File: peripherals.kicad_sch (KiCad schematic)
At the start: 41 parts, among them J8 Conn_01x06_Male, J9 Conn_01x04_MountingPin, U1 MIMX8MM6DVTLZAA, U30 74LVC2G07, U31 TXB0104RUT, U32 TCA9803

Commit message: change USB-UART conn, add new 0402 fp, more pcb work
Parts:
- C143, C144, C145, C146, C147: footprint Capacitor_SMD:C_0402_1005Metric -> qsbc:C_0402_1005Metric
- R100, R101, R102, R103, R104, R105, R106, R107, R108, R109, R110, R111, R112, R113, R114, R115, R116, R117, R118, R119, R120, R121, R122, R123, R124, R125, R126: footprint Resistor_SMD:R_0402_1005Metric -> qsbc:R_0402_1005Metric
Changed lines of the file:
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@@
       (effects (font (size 1.27 1.27)) (justify left))
     )
-    (property "Footprint" "Resistor_SMD:R_0402_1005Metric" (id 2) (at 205.232 40.64 90)
+    (property "Footprint" "qsbc:R_0402_1005Metric" (id 2) (at 205.232 40.64 90)
       (effects (font (size 1.27 1.27)) hide)
     )
@@
       (effects (font (size 1.27 1.27)) (justify left))
     )
-    (property "Footprint" "Resistor_SMD:R_0402_1005Metric" (id 2) (at 125.222 227.33 90)
+    (property "Footprint" "qsbc:R_0402_1005Metric" (id 2) (at 125.222 227.33 90)
       (effects (font (size 1.27 1.27)) hide)
     )
@@
       (effects (font (size 1.27 1.27)) (justify left))
     )
-    (property "Footprint" "Resistor_SMD:R_0402_1005Metric" (id 2) (at 135.382 227.33 90)
+    (property "Footprint" "qsbc:R_0402_1005Metric" (id 2) (at 135.382 227.33 90)
       (effects (font (size 1.27 1.27)) hide)
     )
@@
       (effects (font (size 1.27 1.27)) (justify left))
     )
-    (property "Footprint" "Resistor_SMD:R_0402_1005Metric" (id 2) (at 174.752 40.64 90)
+    (property "Footprint" "qsbc:R_0402_1005Metric" (id 2) (at 174.752 40.64 90)
       (effects (font (size 1.27 1.27)) hide)
     )
@@
       (effects (font (size 1.27 1.27)) (justify left))
     )
-    (property "Footprint" "Resistor_SMD:R_0402_1005Metric" (id 2) (at 168.402 107.95 90)
+    (property "Footprint" "qsbc:R_0402_1005Metric" (id 2) (at 168.402 107.95 90)
       (effects (font (size 1.27 1.27)) hide)
     )
@@
       (effects (font (size 1.27 1.27)) (justify left))
     )
-    (property "Footprint" "Resistor_SMD:R_0402_1005Metric" (id 2) (at 200.152 40.64 90)
+    (property "Footprint" "qsbc:R_0402_1005Metric" (id 2) (at 200.152 40.64 90)
       (effects (font (size 1.27 1.27)) hide)
     )
@@
       (effects (font (size 1.27 1.27)) (justify left))
     )
-    (property "Footprint" "Resistor_SMD:R_0402_1005Metric" (id 2) (at 195.072 40.64 90)
+    (property "Footprint" "qsbc:R_0402_1005Metric" (id 2) (at 195.072 40.64 90)
       (effects (font (size 1.27 1.27)) hide)
     )
@@
       (effects (font (size 1.27 1.27)) (justify left))
     )
-    (property "Footprint" "Capacitor_SMD:C_0402_1005Metric" (id 2) (at 220.6752 118.11 0)
+    (property "Footprint" "qsbc:C_0402_1005Metric" (id 2) (at 220.6752 118.11 0)
       (effects (font (size 1.27 1.27)) hide)
     )
@@
       (effects (font (size 1.27 1.27)) (justify left))
     )
-    (property "Footprint" "Resistor_SMD:R_0402_1005Metric" (id 2) (at 104.902 227.33 90)
+    (property "Footprint" "qsbc:R_0402_1005Metric" (id 2) (at 104.902 227.33 90)
       (effects (font (size 1.27 1.27)) hide)
     )
@@
       (effects (font (size 1.27 1.27)) (justify left))
     )
-    (property "Footprint" "Resistor_SMD:R_0402_1005Metric" (id 2) (at 189.992 40.64 90)
+    (property "Footprint" "qsbc:R_0402_1005Metric" (id 2) (at 189.992 40.64 90)
       (effects (font (size 1.27 1.27)) hide)
     )
@@
       (effects (font (size 1.27 1.27)) (justify left))
     )
-    (property "Footprint" "Resistor_SMD:R_0402_1005Metric" (id 2) (at 174.752 191.77 90)
+    (property "Footprint" "qsbc:R_0402_1005Metric" (id 2) (at 174.752 191.77 90)
       (effects (font (size 1.27 1.27)) hide)
     )
@@
       (effects (font (size 1.27 1.27)) (justify left))
     )
-    (property "Footprint" "Capacitor_SMD:C_0402_1005Metric" (id 2) (at 249.8852 181.61 0)
+    (property "Footprint" "qsbc:C_0402_1005Metric" (id 2) (at 249.8852 181.61 0)
       (effects (font (size 1.27 1.27)) hide)
     )
@@
       (effects (font (size 1.27 1.27)) (justify left))
     )
-    (property "Footprint" "Resistor_SMD:R_0402_1005Metric" (id 2) (at 115.062 227.33 90)
+    (property "Footprint" "qsbc:R_0402_1005Metric" (id 2) (at 115.062 227.33 90)
       (effects (font (size 1.27 1.27)) hide)
     )
@@
       (effects (font (size 1.27 1.27)) (justify left))
     )
-    (property "Footprint" "Resistor_SMD:R_0402_1005Metric" (id 2) (at 145.542 227.33 90)
+    (property "Footprint" "qsbc:R_0402_1005Metric" (id 2) (at 145.542 227.33 90)
       (effects (font (size 1.27 1.27)) hide)
     )
@@
       (effects (font (size 1.27 1.27)) (justify left))
     )
-    (property "Footprint" "Resistor_SMD:R_0402_1005Metric" (id 2) (at 211.582 227.33 90)
+    (property "Footprint" "qsbc:R_0402_1005Metric" (id 2) (at 211.582 227.33 90)
       (effects (font (size 1.27 1.27)) hide)
     )
@@
       (effects (font (size 1.27 1.27)) (justify left))
     )
-    (property "Footprint" "Resistor_SMD:R_0402_1005Metric" (id 2) (at 186.182 107.95 90)
+    (property "Footprint" "qsbc:R_0402_1005Metric" (id 2) (at 186.182 107.95 90)
       (effects (font (size 1.27 1.27)) hide)
     )
@@
       (effects (font (size 1.27 1.27)) (justify left))
     )
-    (property "Footprint" "Capacitor_SMD:C_0402_1005Metric" (id 2) (at 237.1852 181.61 0)
+    (property "Footprint" "qsbc:C_0402_1005Metric" (id 2) (at 237.1852 181.61 0)
       (effects (font (size 1.27 1.27)) hide)
     )
@@
       (effects (font (size 1.27 1.27)) (justify left))
     )
-    (property "Footprint" "Resistor_SMD:R_0402_1005Metric" (id 2) (at 169.672 40.64 90)
+    (property "Footprint" "qsbc:R_0402_1005Metric" (id 2) (at 169.672 40.64 90)
       (effects (font (size 1.27 1.27)) hide)
     )
@@
       (effects (font (size 1.27 1.27)) (justify left))
     )
-    (property "Footprint" "Resistor_SMD:R_0402_1005Metric" (id 2) (at 230.632 40.64 90)
+    (property "Footprint" "qsbc:R_0402_1005Metric" (id 2) (at 230.632 40.64 90)
       (effects (font (size 1.27 1.27)) hide)
     )
@@
       (effects (font (size 1.27 1.27)) (justify left))
     )
-    (property "Footprint" "Resistor_SMD:R_0402_1005Metric" (id 2) (at 201.422 227.33 90)
+    (property "Footprint" "qsbc:R_0402_1005Metric" (id 2) (at 201.422 227.33 90)
       (effects (font (size 1.27 1.27)) hide)
     )
@@
       (effects (font (size 1.27 1.27)) (justify left))
     )
-    (property "Footprint" "Resistor_SMD:R_0402_1005Metric" (id 2) (at 220.472 40.64 90)
+    (property "Footprint" "qsbc:R_0402_1005Metric" (id 2) (at 220.472 40.64 90)
       (effects (font (size 1.27 1.27)) hide)
     )
@@
       (effects (font (size 1.27 1.27)) (justify left))
     )
-    (property "Footprint" "Resistor_SMD:R_0402_1005Metric" (id 2) (at 179.832 40.64 90)
+    (property "Footprint" "qsbc:R_0402_1005Metric" (id 2) (at 179.832 40.64 90)
       (effects (font (size 1.27 1.27)) hide)
     )
@@
       (effects (font (size 1.27 1.27)) (justify left))
     )
-    (property "Footprint" "Capacitor_SMD:C_0402_1005Metric" (id 2) (at 250.2044 231.1951 0)
+    (property "Footprint" "qsbc:C_0402_1005Metric" (id 2) (at 250.2044 231.1951 0)
       (effects (font (size 1.27 1.27)) hide)
     )
@@
       (effects (font (size 1.27 1.27)) (justify left))
     )
-    (property "Footprint" "Capacitor_SMD:C_0402_1005Metric" (id 2) (at 237.5044 231.1951 0)
+    (property "Footprint" "qsbc:C_0402_1005Metric" (id 2) (at 237.5044 231.1951 0)
       (effects (font (size 1.27 1.27)) hide)
     )
@@
       (effects (font (size 1.27 1.27)) (justify left))
     )
-    (property "Footprint" "Resistor_SMD:R_0402_1005Metric" (id 2) (at 225.552 40.64 90)
+    (property "Footprint" "qsbc:R_0402_1005Metric" (id 2) (at 225.552 40.64 90)
       (effects (font (size 1.27 1.27)) hide)
     )
@@
       (effects (font (size 1.27 1.27)) (justify left))
     )
-    (property "Footprint" "Resistor_SMD:R_0402_1005Metric" (id 2) (at 215.392 40.64 90)
+    (property "Footprint" "qsbc:R_0402_1005Metric" (id 2) (at 215.392 40.64 90)
       (effects (font (size 1.27 1.27)) hide)
     )
@@
       (effects (font (size 1.27 1.27)) (justify left))
     )
-    (property "Footprint" "Resistor_SMD:R_0402_1005Metric" (id 2) (at 210.312 40.64 90)
+    (property "Footprint" "qsbc:R_0402_1005Metric" (id 2) (at 210.312 40.64 90)
       (effects (font (size 1.27 1.27)) hide)
     )
@@
       (effects (font (size 1.27 1.27)) (justify left))
     )
-    (property "Footprint" "Resistor_SMD:R_0402_1005Metric" (id 2) (at 159.512 40.64 90)
+    (property "Footprint" "qsbc:R_0402_1005Metric" (id 2) (at 159.512 40.64 90)
       (effects (font (size 1.27 1.27)) hide)
     )
@@
       (effects (font (size 1.27 1.27)) (justify left))
     )
-    (property "Footprint" "Resistor_SMD:R_0402_1005Metric" (id 2) (at 164.592 40.64 90)
+    (property "Footprint" "qsbc:R_0402_1005Metric" (id 2) (at 164.592 40.64 90)
       (effects (font (size 1.27 1.27)) hide)
     )
@@
       (effects (font (size 1.27 1.27)) (justify left))
     )
-    (property "Footprint" "Resistor_SMD:R_0402_1005Metric" (id 2) (at 184.912 40.64 90)
+    (property "Footprint" "qsbc:R_0402_1005Metric" (id 2) (at 184.912 40.64 90)
       (effects (font (size 1.27 1.27)) hide)
     )
@@
       (effects (font (size 1.27 1.27)) (justify left))
     )
-    (property "Footprint" "Resistor_SMD:R_0402_1005Metric" (id 2) (at 94.742 227.33 90)
+    (property "Footprint" "qsbc:R_0402_1005Metric" (id 2) (at 94.742 227.33 90)
       (effects (font (size 1.27 1.27)) hide)
     )
@@
       (effects (font (size 1.27 1.27)) (justify left))
     )
-    (property "Footprint" "Resistor_SMD:R_0402_1005Metric" (id 2) (at 235.712 40.64 90)
+    (property "Footprint" "qsbc:R_0402_1005Metric" (id 2) (at 235.712 40.64 90)
       (effects (font (size 1.27 1.27)) hide)
     )

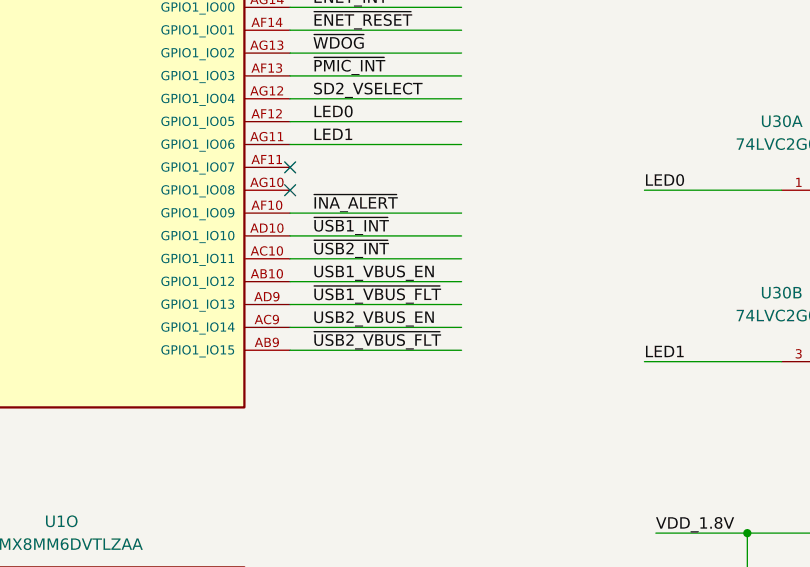
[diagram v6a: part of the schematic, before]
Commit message: swap usb ctrl signals for layout
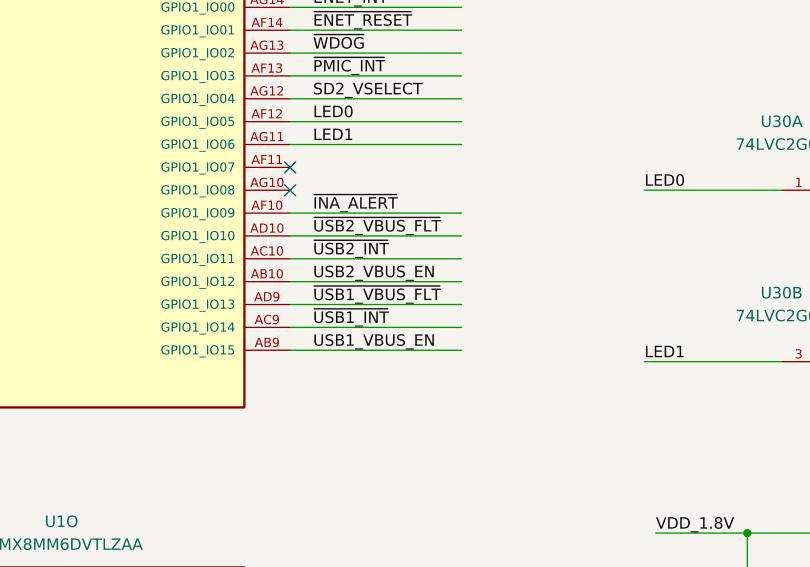
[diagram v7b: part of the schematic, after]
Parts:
- TP27: footprint TestPoint:TestPoint_Pad_D1.0mm -> qsbc:TestPoint_Pad_D0.4mm
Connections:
- net USB1_VBUS_EN: now also U1.AB9 (GPIO1_IO15); no longer U1.AB10 (GPIO1_IO12)
- net USB2_VBUS_EN: now also U1.AB10 (GPIO1_IO12); no longer U1.AC9 (GPIO1_IO14)
- net ~{USB1_INT}: now also U1.AC9 (GPIO1_IO14); no longer U1.AD10 (GPIO1_IO10)
- net ~{USB2_VBUS_FLT}: now also U1.AD10 (GPIO1_IO10); no longer U1.AB9 (GPIO1_IO15)
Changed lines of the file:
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@@
     (effects (font (size 1.27 1.27)) (justify left bottom))
   )
-  (label "~{USB2_VBUS_FLT}" (at 80.01 142.24 0)
+  (label "~{USB2_VBUS_FLT}" (at 80.01 129.54 0)
     (effects (font (size 1.27 1.27)) (justify left bottom))
   )
@@
     (effects (font (size 1.27 1.27)) (justify left bottom))
   )
-  (label "USB2_VBUS_EN" (at 80.01 139.7 0)
+  (label "USB2_VBUS_EN" (at 80.01 134.62 0)
     (effects (font (size 1.27 1.27)) (justify left bottom))
   )
@@
     (effects (font (size 1.27 1.27)) (justify left bottom))
   )
-  (label "USB1_VBUS_EN" (at 80.01 134.62 0)
+  (label "USB1_VBUS_EN" (at 80.01 142.24 0)
     (effects (font (size 1.27 1.27)) (justify left bottom))
   )
@@
     (effects (font (size 1.27 1.27)) (justify left bottom))
   )
-  (label "~{USB1_INT}" (at 80.01 129.54 0)
+  (label "~{USB1_INT}" (at 80.01 139.7 0)
     (effects (font (size 1.27 1.27)) (justify left bottom))
   )
@@
       (effects (font (size 1.27 1.27)) (justify left))
     )
-    (property "Footprint" "TestPoint:TestPoint_Pad_D1.0mm" (id 2) (at 181.61 172.72 0)
+    (property "Footprint" "qsbc:TestPoint_Pad_D0.4mm" (id 2) (at 181.61 172.72 0)
       (effects (font (size 1.27 1.27)) hide)
     )

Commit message: pmic routing almost done
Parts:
- removed C143: 0.1uF, qsbc:C_0402_1005Metric, symbol Device:C
- removed D5: LED_Green, LED_SMD:LED_0603_1608Metric, symbol Device:LED
- removed D6: LED_Red, LED_SMD:LED_0603_1608Metric, symbol Device:LED
- removed R108, R114: 2.2K, qsbc:R_0402_1005Metric, symbol Device:R
- removed U30: 74LVC2G07, Package_TO_SOT_SMD:SOT-886, symbol 74xGxx:74LVC2G07
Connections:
- net SD2_VSELECT: now also U1.AF10 (GPIO1_IO09); no longer U1.AG12 (GPIO1_IO04)
- net ~{INA_ALERT}: now also U1.AF13 (GPIO1_IO03); no longer U1.AF10 (GPIO1_IO09)
- net ~{PMIC_INT}: now also U1.AG12 (GPIO1_IO04); no longer U1.AF13 (GPIO1_IO03)
- net LED0: no longer names the net of U1.AF12 (GPIO1_IO05)
- net LED1: no longer names the net of U1.AG11 (GPIO1_IO06)
- net VCC renamed VDD_1.8V
- no-connect marks 39 -> 41
